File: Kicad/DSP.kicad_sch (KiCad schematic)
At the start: 2 parts, among them U1 MIMXRT685SFVKB, X1 ECS-2520MV-xxx-xx

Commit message: power section
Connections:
- net VDD1V8 is gone; now on net +1V8: U1.B11 (VDD1V8), U1.C16 (VDD1V8), U1.C17 (VDD1V8), U1.E15 (VDD1V8), U1.F13 (VDD1V8), U1.G14 (VDD1V8), U1.L4 (VDD1V8), U1.R15 (VDD1V8)
- net VDDIO_1 is gone; now on net +3V3: U1.E10 (VDDIO_1), U1.E6 (VDDIO_1), U1.E8 (VDDIO_1), U1.H13 (VDDIO_1), U1.H14 (VDDIO_1), U1.K13 (VDDIO_1), U1.L14 (VDDIO_1)
- net VDDIO_2 is gone; now on net +3V3: U1.N12 (VDDIO_2), U1.P11 (VDDIO_2), U1.P12 (VDDIO_2)
- net VDD_AO1V8 is gone; now on net +1V8: U1.C13 (VDD_AO1V8), U1.D13 (VDD_AO1V8)
- net +1V8: now reaches U1.A13 (VDD1V8_1)
- net +1V8: now also U1.E4 (VDDA_ADC1V8)
- net VDDIO_0 renamed +3V3
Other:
- note added: "Each VDDIO supply pin may be supplied at different voltage levels between 1.71 V to 3.6 V."
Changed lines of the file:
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@@
 (kicad_sch (version 20211123) (generator eeschema)
   (paper "A4")
+  (junction (at 93.98 39.37) (diameter 0) (color 0 0 0 0)
+  )
+  (junction (at 72.39 39.37) (diameter 0) (color 0 0 0 0)
+  )
+  (junction (at 67.31 39.37) (diameter 0) (color 0 0 0 0)
+  )
+  (junction (at 83.82 39.37) (diameter 0) (color 0 0 0 0)
+  )
   (junction (at 77.47 109.22) (diameter 0) (color 0 0 0 0)
   )
+  (junction (at 88.9 39.37) (diameter 0) (color 0 0 0 0)
+  )
   (wire (pts (xy 156.21 53.34) (xy 165.1 53.34))
     (stroke (width 0) (type default) (color 0 0 0 0))
   )
-  (wire (pts (xy 29.21 95.25) (xy 41.91 95.25))
+  (wire (pts (xy 88.9 39.37) (xy 93.98 39.37))
+    (stroke (width 0) (type default) (color 0 0 0 0))
+  )
+  (wire (pts (xy 83.82 39.37) (xy 88.9 39.37))
+    (stroke (width 0) (type default) (color 0 0 0 0))
+  )
+  (wire (pts (xy 93.98 39.37) (xy 99.06 39.37))
     (stroke (width 0) (type default) (color 0 0 0 0))
   )
@@
     (stroke (width 0) (type default) (color 0 0 0 0))
   )
+  (wire (pts (xy 39.37 95.25) (xy 41.91 95.25))
+    (stroke (width 0) (type default) (color 0 0 0 0))
+  )
   (wire (pts (xy 104.14 114.3) (xy 113.03 114.3))
     (stroke (width 0) (type default) (color 0 0 0 0))
@@
     (stroke (width 0) (type default) (color 0 0 0 0))
   )
+  (wire (pts (xy 77.47 39.37) (xy 72.39 39.37))
+    (stroke (width 0) (type default) (color 0 0 0 0))
+  )
   (wire (pts (xy 156.21 45.72) (xy 165.1 45.72))
     (stroke (width 0) (type default) (color 0 0 0 0))
@@
     (stroke (width 0) (type default) (color 0 0 0 0))
   )
-  (wire (pts (xy 29.21 97.79) (xy 41.91 97.79))
+  (wire (pts (xy 39.37 97.79) (xy 41.91 97.79))
     (stroke (width 0) (type default) (color 0 0 0 0))
   )
@@
     (stroke (width 0) (type default) (color 0 0 0 0))
   )
+  (wire (pts (xy 72.39 39.37) (xy 67.31 39.37))
+    (stroke (width 0) (type default) (color 0 0 0 0))
+  )
   (wire (pts (xy 133.35 83.82) (xy 116.84 83.82))
     (stroke (width 0) (type default) (color 0 0 0 0))
   )
-  (wire (pts (xy 29.21 92.71) (xy 41.91 92.71))
+  (wire (pts (xy 39.37 92.71) (xy 41.91 92.71))
     (stroke (width 0) (type default) (color 0 0 0 0))
   )
@@
     (stroke (width 0) (type default) (color 0 0 0 0))
   )
+  (wire (pts (xy 83.82 34.29) (xy 83.82 39.37))
+    (stroke (width 0) (type default) (color 0 0 0 0))
+  )
   (wire (pts (xy 29.21 66.04) (xy 41.91 66.04))
     (stroke (width 0) (type default) (color 0 0 0 0))
@@
     (stroke (width 0) (type default) (color 0 0 0 0))
   )
+  (wire (pts (xy 67.31 39.37) (xy 67.31 34.29))
+    (stroke (width 0) (type default) (color 0 0 0 0))
+  )
   (wire (pts (xy 156.21 50.8) (xy 165.1 50.8))
     (stroke (width 0) (type default) (color 0 0 0 0))
@@
     (stroke (width 0) (type default) (color 0 0 0 0))
   )
-  (wire (pts (xy 29.21 90.17) (xy 41.91 90.17))
+  (wire (pts (xy 39.37 90.17) (xy 41.91 90.17))
     (stroke (width 0) (type default) (color 0 0 0 0))
   )
@@
     (stroke (width 0) (type default) (color 0 0 0 0))
   )
+  (text "Each VDDIO supply pin may be supplied at different voltage levels \nbetween 1.71 V to 3.6 V."
+    (at 58.42 25.4 0)
+    (effects (font (size 1 1)) (justify left bottom))
+  )
   (label "FC_05" (at 156.21 45.72 0)
     (effects (font (size 1.27 1.27)) (justify left bottom))
@@
     (effects (font (size 1.27 1.27)) (justify right bottom))
   )
-  (label "USB1_VDD3V3" (at 29.21 97.79 0)
-    (effects (font (size 1.27 1.27)) (justify left bottom))
-  )
   (label "FC_00_I2S_CLK" (at 140.97 33.02 0)
     (effects (font (size 1.27 1.27)) (justify left bottom))
@@
     (effects (font (size 1.27 1.27)) (justify right bottom))
   )
-  (label "USB1_DP" (at 29.21 92.71 0)
-    (effects (font (size 1.27 1.27)) (justify left bottom))
-  )
-  (label "USB1_DM" (at 29.21 90.17 0)
-    (effects (font (size 1.27 1.27)) (justify left bottom))
-  )
   (label "MODE0" (at 29.21 68.58 0)
     (effects (font (size 1.27 1.27)) (justify left bottom))
@@
     (effects (font (size 1.27 1.27)) (justify right bottom))
   )
-  (label "USB1_VBUS" (at 29.21 95.25 0)
-    (effects (font (size 1.27 1.27)) (justify left bottom))
-  )
   (label "FC_01_I2S_WS" (at 140.97 35.56 0)
     (effects (font (size 1.27 1.27)) (justify left bottom))
@@
   (label "FC_03" (at 156.21 40.64 0)
     (effects (font (size 1.27 1.27)) (justify left bottom))
+  )
+  (hierarchical_label "USB1_VBUS" (shape input) (at 39.37 95.25 180)
+    (effects (font (size 1.27 1.27)) (justify right))
+  )
+  (hierarchical_label "USB1_DP" (shape bidirectional) (at 39.37 92.71 180)
+    (effects (font (size 1.27 1.27)) (justify right))
+  )
+  (hierarchical_label "USB1_DM" (shape bidirectional) (at 39.37 90.17 180)
+    (effects (font (size 1.27 1.27)) (justify right))
+  )
+  (hierarchical_label "USB1_VDD3V3" (shape input) (at 39.37 97.79 180)
+    (effects (font (size 1.27 1.27)) (justify right))
   )
   (symbol (lib_id "power:GND") (at 77.47 113.03 0) (unit 1)
@@
     (pin "4")
   )
+  (symbol (lib_id "power:+1V8") (at 83.82 34.29 0) (unit 1)
+    (in_bom yes) (on_board yes) (fields_autoplaced)
+    (property "Reference" "#PWR03" (id 0) (at 83.82 38.1 0)
+      (effects (font (size 1.27 1.27)) hide)
+    )
+    (property "Value" "+1V8" (id 1) (at 83.82 29.21 0))
+    (property "Footprint" "" (id 2) (at 83.82 34.29 0)
+      (effects (font (size 1.27 1.27)) hide)
+    )
+    (property "Datasheet" "" (id 3) (at 83.82 34.29 0)
+      (effects (font (size 1.27 1.27)) hide)
+    )
+    (pin "1")
+  )
+  (symbol (lib_id "power:+3V3") (at 67.31 34.29 0) (unit 1)
+    (in_bom yes) (on_board yes) (fields_autoplaced)
+    (property "Reference" "#PWR01" (id 0) (at 67.31 38.1 0)
+      (effects (font (size 1.27 1.27)) hide)
+    )
+    (property "Value" "+3V3" (id 1) (at 67.31 29.21 0))
+    (property "Footprint" "" (id 2) (at 67.31 34.29 0)
+      (effects (font (size 1.27 1.27)) hide)
+    )
+    (property "Datasheet" "" (id 3) (at 67.31 34.29 0)
+      (effects (font (size 1.27 1.27)) hide)
+    )
+    (pin "1")
+  )
   (symbol (lib_id "project_sym_lib:MIMXRT685SFVKB") (at 80.01 76.2 0) (unit 1)

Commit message: working on DSP
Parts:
- U1: footprint project_footprints:BGA-289_17x17_9.0x9.0mm_v2 -> project_footprints:MIMXRT685SFVKB
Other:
- moved on the sheet: X1

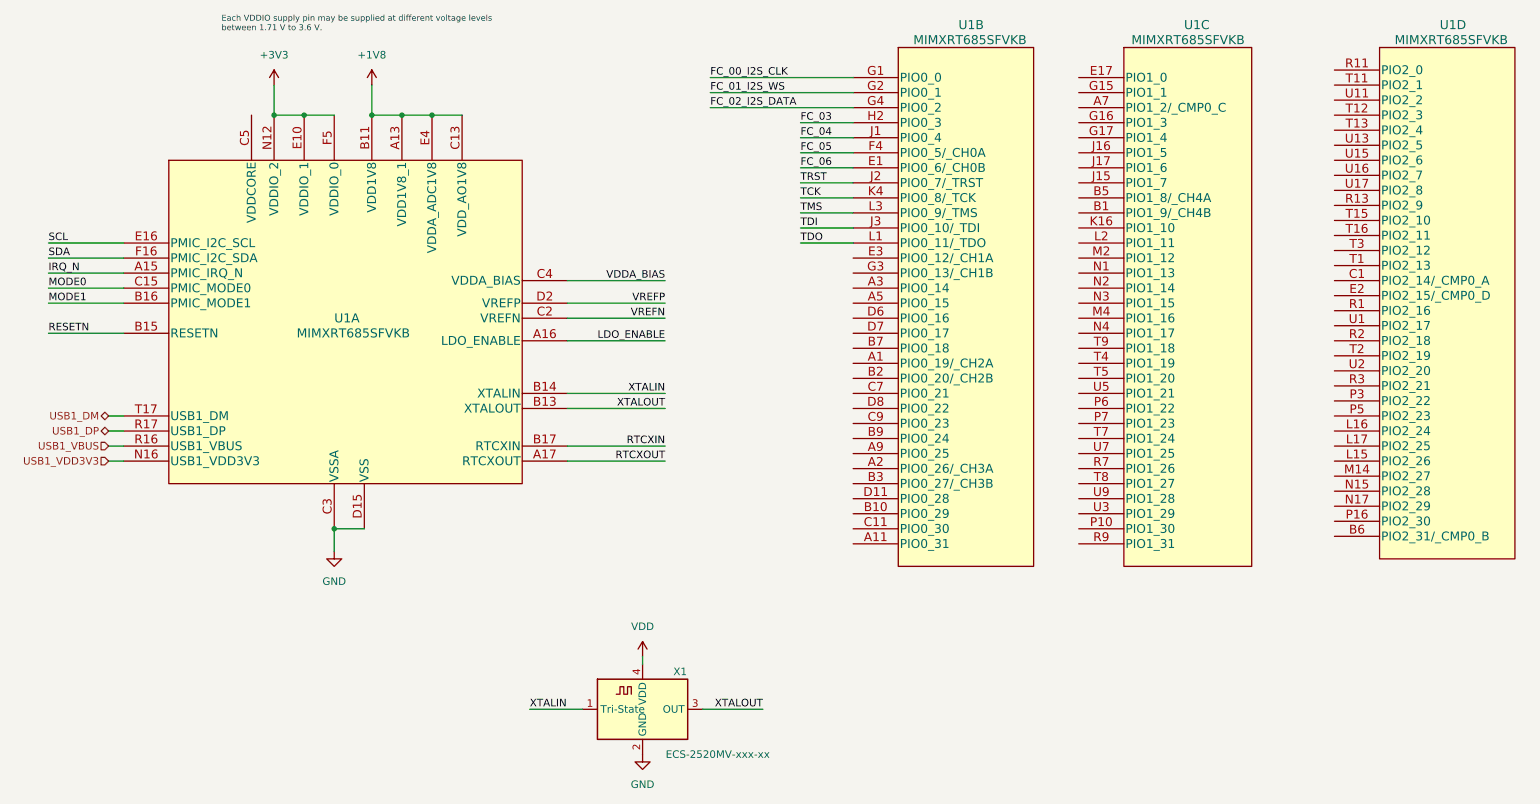
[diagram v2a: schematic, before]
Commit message: updated DAC circut
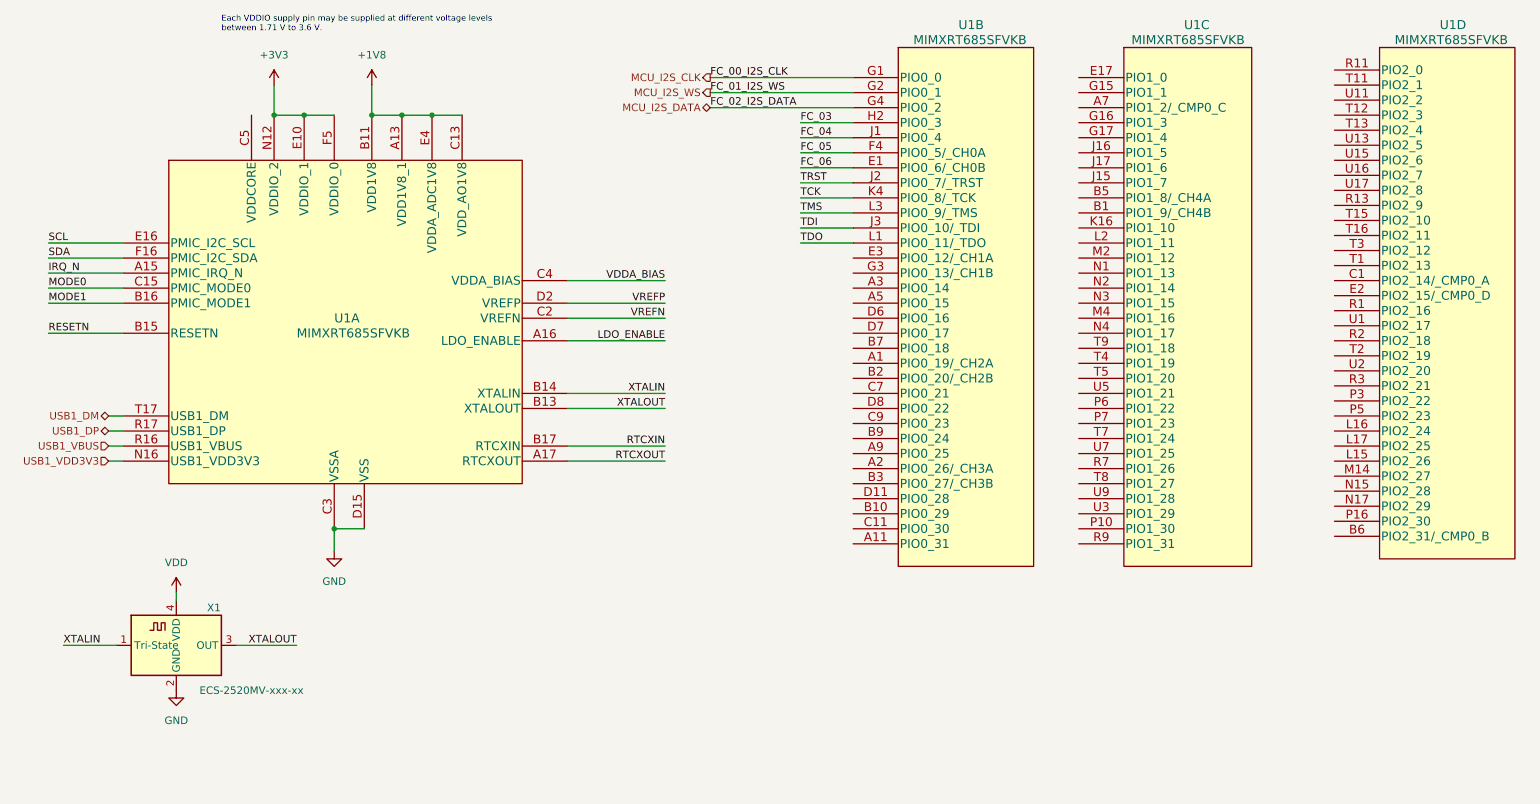
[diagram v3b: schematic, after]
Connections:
- net FC_00_I2S_CLK renamed MCU_I2S_CLK
- net FC_01_I2S_WS renamed MCU_I2S_WS
- net FC_02_I2S_DATA renamed MCU_I2S_DATA
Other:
- moved on the sheet: X1
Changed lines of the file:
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@@
     (stroke (width 0) (type default) (color 0 0 0 0))
   )
-  (wire (pts (xy 110.49 139.7) (xy 119.38 139.7))
+  (wire (pts (xy 31.75 128.905) (xy 40.64 128.905))
     (stroke (width 0) (type default) (color 0 0 0 0))
   )
@@
     (stroke (width 0) (type default) (color 0 0 0 0))
   )
-  (wire (pts (xy 149.86 139.7) (xy 139.7 139.7))
+  (wire (pts (xy 71.12 128.905) (xy 60.96 128.905))
     (stroke (width 0) (type default) (color 0 0 0 0))
   )
@@
     (stroke (width 0) (type default) (color 0 0 0 0))
   )
-  (wire (pts (xy 129.54 130.81) (xy 129.54 132.08))
+  (wire (pts (xy 50.8 120.015) (xy 50.8 121.285))
     (stroke (width 0) (type default) (color 0 0 0 0))
   )
@@
     (effects (font (size 1.27 1.27)) (justify left bottom))
   )
-  (label "XTALOUT" (at 149.86 139.7 180)
+  (label "XTALOUT" (at 71.12 128.905 180)
     (effects (font (size 1.27 1.27)) (justify right bottom))
   )
@@
     (effects (font (size 1.27 1.27)) (justify left bottom))
   )
-  (label "XTALIN" (at 110.49 139.7 0)
+  (label "XTALIN" (at 31.75 128.905 0)
     (effects (font (size 1.27 1.27)) (justify left bottom))
   )
@@
     (effects (font (size 1.27 1.27)) (justify left bottom))
   )
+  (hierarchical_label "MCU_I2S_WS" (shape output) (at 140.97 35.56 180)
+    (effects (font (size 1.27 1.27)) (justify right))
+  )
   (hierarchical_label "USB1_VBUS" (shape input) (at 39.37 95.25 180)
     (effects (font (size 1.27 1.27)) (justify right))
   )
+  (hierarchical_label "MCU_I2S_CLK" (shape output) (at 140.97 33.02 180)
+    (effects (font (size 1.27 1.27)) (justify right))
+  )
   (hierarchical_label "USB1_DP" (shape bidirectional) (at 39.37 92.71 180)
+    (effects (font (size 1.27 1.27)) (justify right))
+  )
+  (hierarchical_label "MCU_I2S_DATA" (shape bidirectional) (at 140.97 38.1 180)
     (effects (font (size 1.27 1.27)) (justify right))
   )
@@
     (pin "U2")
   )
-  (symbol (lib_id "power:VDD") (at 129.54 130.81 0) (unit 1)
+  (symbol (lib_id "power:VDD") (at 50.8 120.015 0) (unit 1)
     (in_bom yes) (on_board yes) (fields_autoplaced)
-    (property "Reference" "#PWR04" (id 0) (at 129.54 134.62 0)
-      (effects (font (size 1.27 1.27)) hide)
-    )
-    (property "Value" "VDD" (id 1) (at 129.54 125.73 0))
-    (property "Footprint" "" (id 2) (at 129.54 130.81 0)
-      (effects (font (size 1.27 1.27)) hide)
-    )
-    (property "Datasheet" "" (id 3) (at 129.54 130.81 0)
+    (property "Reference" "#PWR04" (id 0) (at 50.8 123.825 0)
+      (effects (font (size 1.27 1.27)) hide)
+    )
+    (property "Value" "VDD" (id 1) (at 50.8 114.935 0))
+    (property "Footprint" "" (id 2) (at 50.8 120.015 0)
+      (effects (font (size 1.27 1.27)) hide)
+    )
+    (property "Datasheet" "" (id 3) (at 50.8 120.015 0)
       (effects (font (size 1.27 1.27)) hide)
     )
     (pin "1")
   )
-  (symbol (lib_id "Oscillator:ECS-2520MV-xxx-xx") (at 129.54 139.7 0) (unit 1)
+  (symbol (lib_id "Oscillator:ECS-2520MV-xxx-xx") (at 50.8 128.905 0) (unit 1)
     (in_bom yes) (on_board yes)
-    (property "Reference" "X1" (id 0) (at 135.89 133.35 0))
-    (property "Value" "ECS-2520MV-xxx-xx" (id 1) (at 142.24 147.32 0))
-    (property "Footprint" "Oscillator:Oscillator_SMD_ECS_2520MV-xxx-xx-4Pin_2.5x2.0mm" (id 2) (at 140.97 148.59 0)
-      (effects (font (size 1.27 1.27)) hide)
-    )
-    (property "Datasheet" "https://www.ecsxtal.com/store/pdf/ECS-2520MV.pdf" (id 3) (at 125.095 136.525 0)
+    (property "Reference" "X1" (id 0) (at 57.15 122.555 0))
+    (property "Value" "ECS-2520MV-xxx-xx" (id 1) (at 63.5 136.525 0))
+    (property "Footprint" "Oscillator:Oscillator_SMD_ECS_2520MV-xxx-xx-4Pin_2.5x2.0mm" (id 2) (at 62.23 137.795 0)
+      (effects (font (size 1.27 1.27)) hide)
+    )
+    (property "Datasheet" "https://www.ecsxtal.com/store/pdf/ECS-2520MV.pdf" (id 3) (at 46.355 125.73 0)
       (effects (font (size 1.27 1.27)) hide)
     )
@@
     (pin "U2")
   )
-  (symbol (lib_id "power:GND") (at 129.54 147.32 0) (unit 1)
+  (symbol (lib_id "power:GND") (at 50.8 136.525 0) (unit 1)
     (in_bom yes) (on_board yes) (fields_autoplaced)
-    (property "Reference" "#PWR05" (id 0) (at 129.54 153.67 0)
-      (effects (font (size 1.27 1.27)) hide)
-    )
-    (property "Value" "GND" (id 1) (at 129.54 152.4 0))
-    (property "Footprint" "" (id 2) (at 129.54 147.32 0)
-      (effects (font (size 1.27 1.27)) hide)
-    )
-    (property "Datasheet" "" (id 3) (at 129.54 147.32 0)
-      (effects (font (size 1.27 1.27)) hide)
-    )
+    (property "Reference" "#PWR05" (id 0) (at 50.8 142.875 0)
+      (effects (font (size 1.27 1.27)) hide)
+    )
+    (property "Value" "GND" (id 1) (at 50.8 141.605 0))
+    (property "Footprint" "" (id 2) (at 50.8 136.525 0)
+      (effects (font (size 1.27 1.27)) hide)
+    )
+    (property "Datasheet" "" (id 3) (at 50.8 136.525 0)
+      (effects (font (size 1.27 1.27)) hide)
+    )
